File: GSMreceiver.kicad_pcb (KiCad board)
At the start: 2 copper layers, 69 x 83 mm, 136 parts, among them J1 Conn_01x06_Pin, J10 Conn_01x05, J11 Conn_DEGSON_01x02_Pin, J2 Conn_02x02_2.54, J3 Conn_DEGSON_01x02_Pin, J4 Conn_DEGSON_01x02_Pin, J5 Conn_DEGSON_01x02_Pin, J6 Conn_DEGSON_01x02_Pin, J7 Conn_DEGSON_01x02_Pin, J8 1042240820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

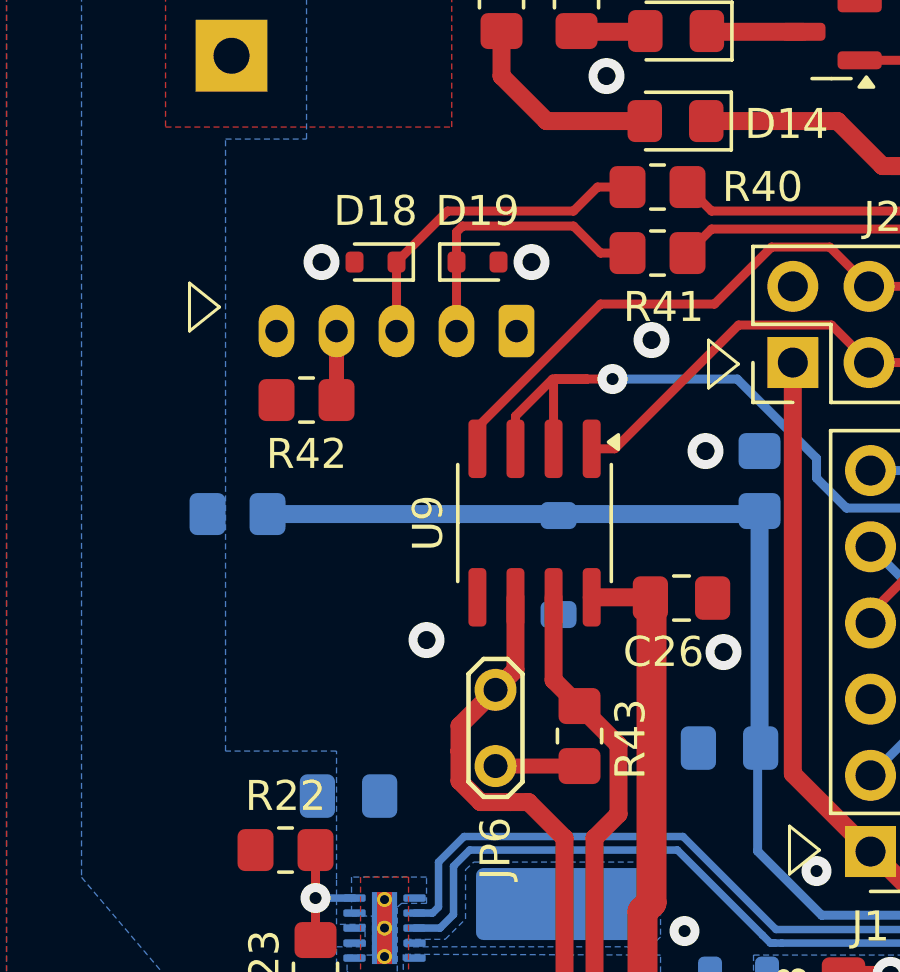
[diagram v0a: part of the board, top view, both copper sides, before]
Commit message: USB pinout fixed
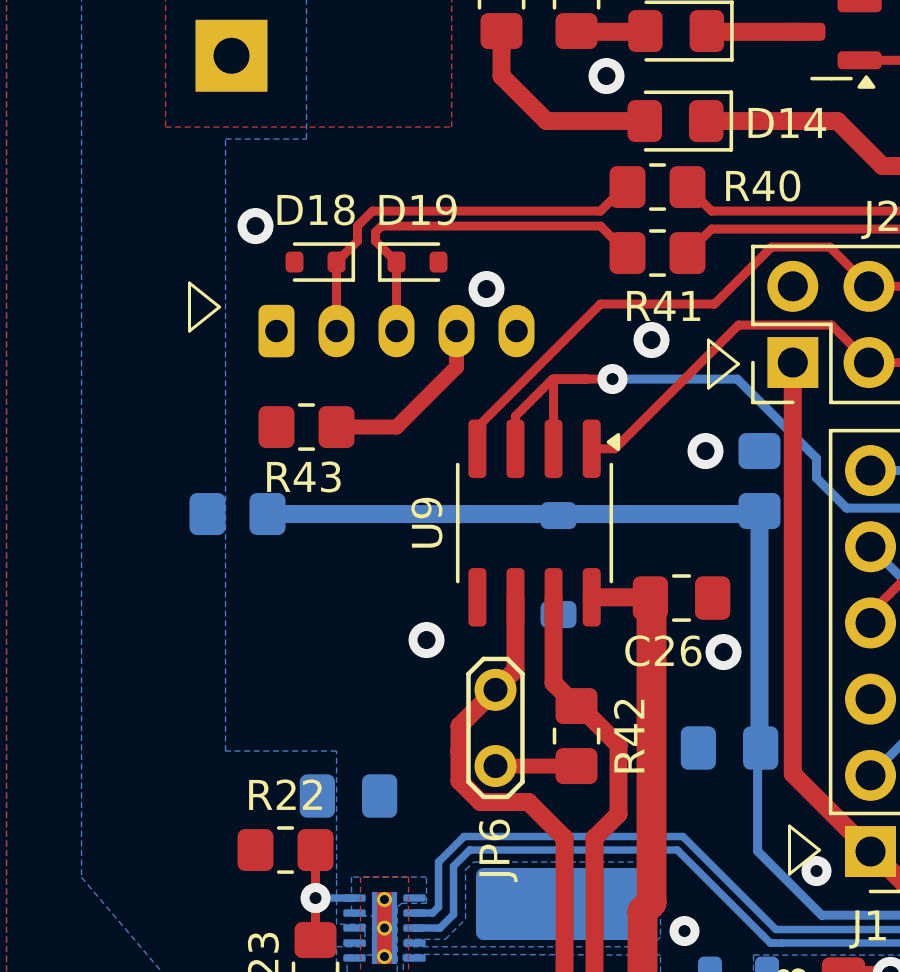
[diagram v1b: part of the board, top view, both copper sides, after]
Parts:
- L1: value 10uH -> MLZ2012M100WT000
- R42: value 5k1 -> 680
- R43: value 680 -> 5k1
- moved R42 14.4 mm to (47.5, 72.5), turned to -90 degrees
- moved R43 13.7 mm to (38.5, 62.2), turned to 180 degrees
- moved J10 8.00 mm to (37.5, 59.0), turned to 0 degrees
- moved D18 2.00 mm to (38.8, 56.7)
- moved D19 2.00 mm to (42.2, 56.7)
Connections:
- J10 pad 1: unconnected-(J10-Pin_1-Pad1) -> GNDD
- J10 pad 2: /Interface/D- -> /Interface/D+
- J10 pad 3: /Interface/D+ -> /Interface/D-
- J10 pad 5: GNDD -> unconnected-(J10-Pin_5-Pad5)
- R42 pad 1: Net-(J10-Pin_4) -> /Interface/RS485_N
- R42 pad 2: GNDD -> Net-(JP6-A)
- R43 pad 1: /Interface/RS485_N -> Net-(J10-Pin_4)
- R43 pad 2: Net-(JP6-A) -> GNDD
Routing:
- net Net-(J10-Pin_4): track 2.34 -> 6.03 mm
- net /Interface/D-: track 9.46 -> 12.4 mm
- net /Interface/D+: track 11.0 -> 13.3 mm

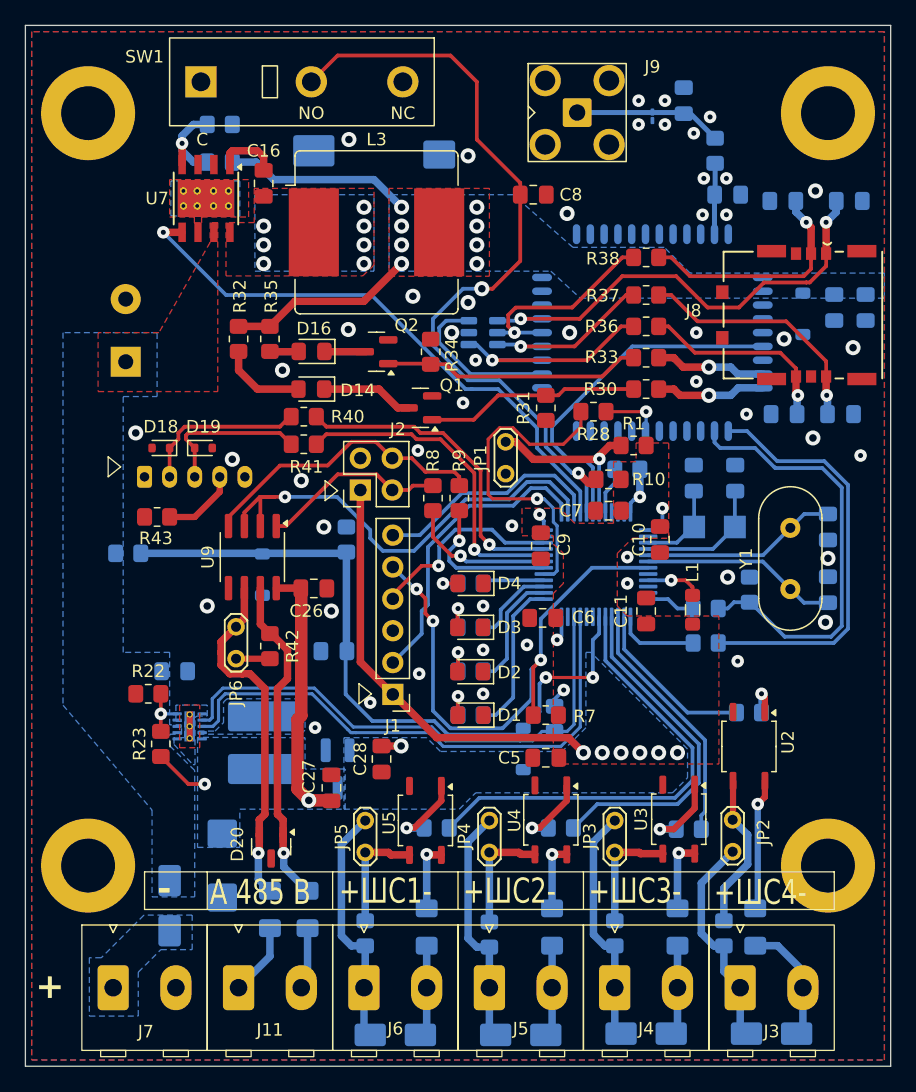
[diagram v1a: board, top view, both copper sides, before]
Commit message: Minor changes in PCB for manufacturing
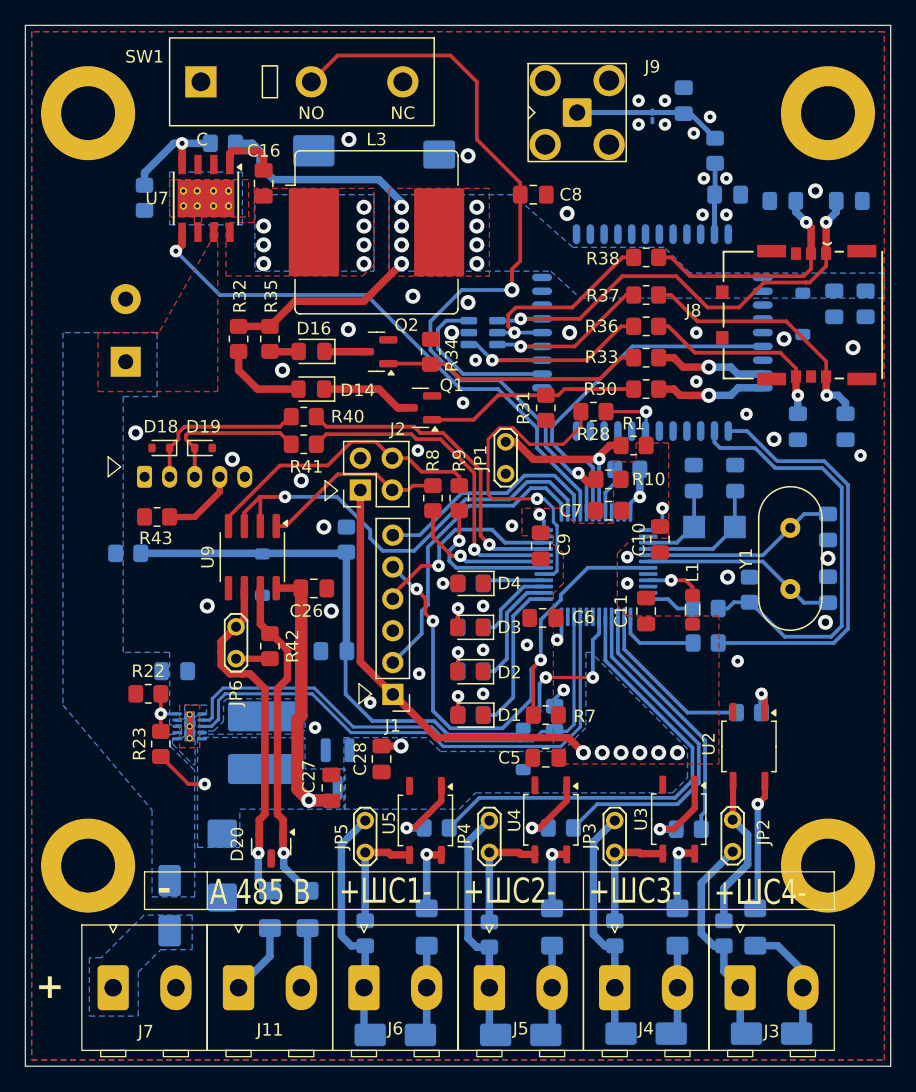
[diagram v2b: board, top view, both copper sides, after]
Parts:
- moved R24 8.38 mm to (37.5, 36.8), turned to 90 degrees
- moved R25 1.52 mm to (43.8, 32.4)
- moved C24 1.49 mm to (89.6, 55.0), turned to 90 degrees
- moved C23 1.08 mm to (93.4, 55.0), turned to 90 degrees
- moved C18 0.30 mm to (92.5, 45.2)
- moved C19 0.30 mm to (95.0, 45.2)
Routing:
- net /TAMPER: track 63.5 -> 65.0 mm
- net /4V_ENABLE: track 45.9 -> 44.5 mm
- net +4V: track 30.1 -> 31.4 mm
- net Net-(U7-VSENSE): track 7.64 -> 8.92 mm
- net /RFmodule/CARD_CLK: track 19.8 -> 20.9 mm
